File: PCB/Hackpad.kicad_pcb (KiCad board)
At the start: 2 copper layers, 86 x 50 mm, 11 parts, among them SW1 SW_Push, SW2 SW_Push, SW3 SW_Push, SW4 SW_Push, SW5 RotaryEncoder, U1 XIAO-RP2040-DIP, U2 SSD1306

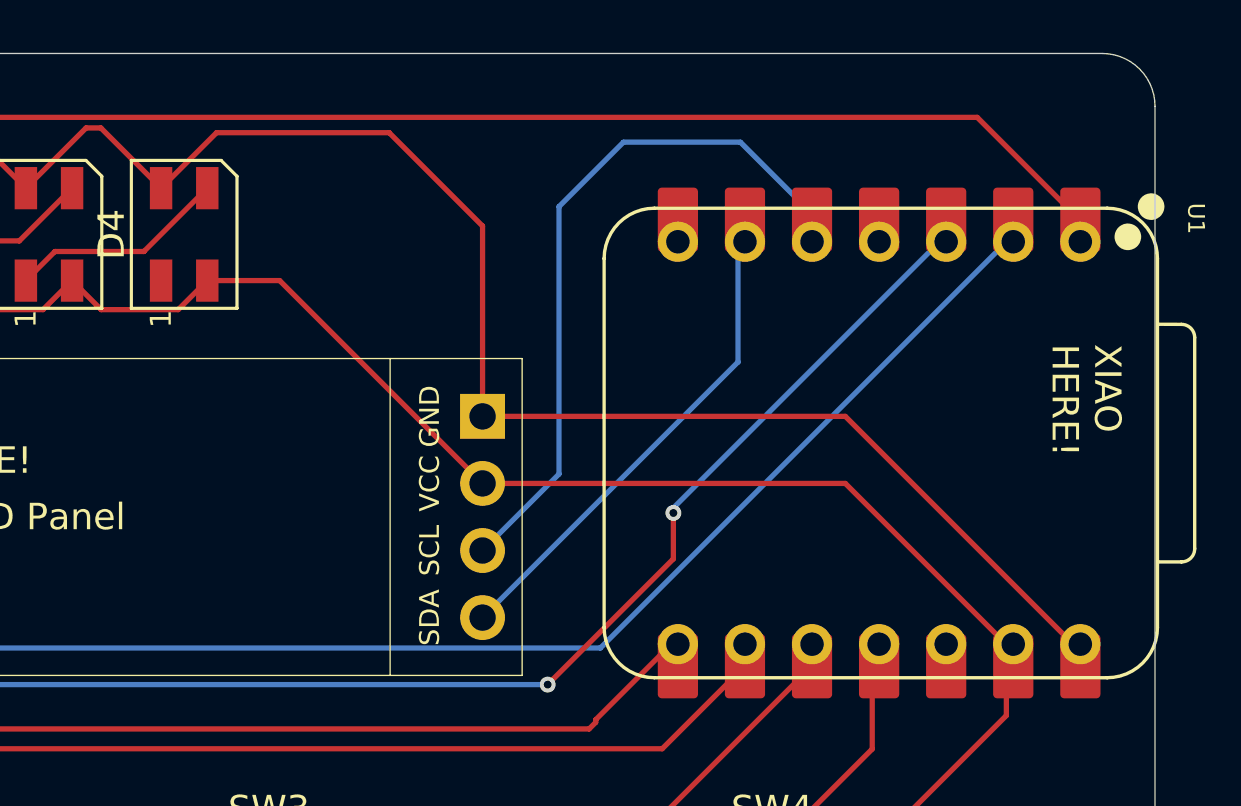
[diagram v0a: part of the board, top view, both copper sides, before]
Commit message: Connected the OLED to 3.3V instead of 5V
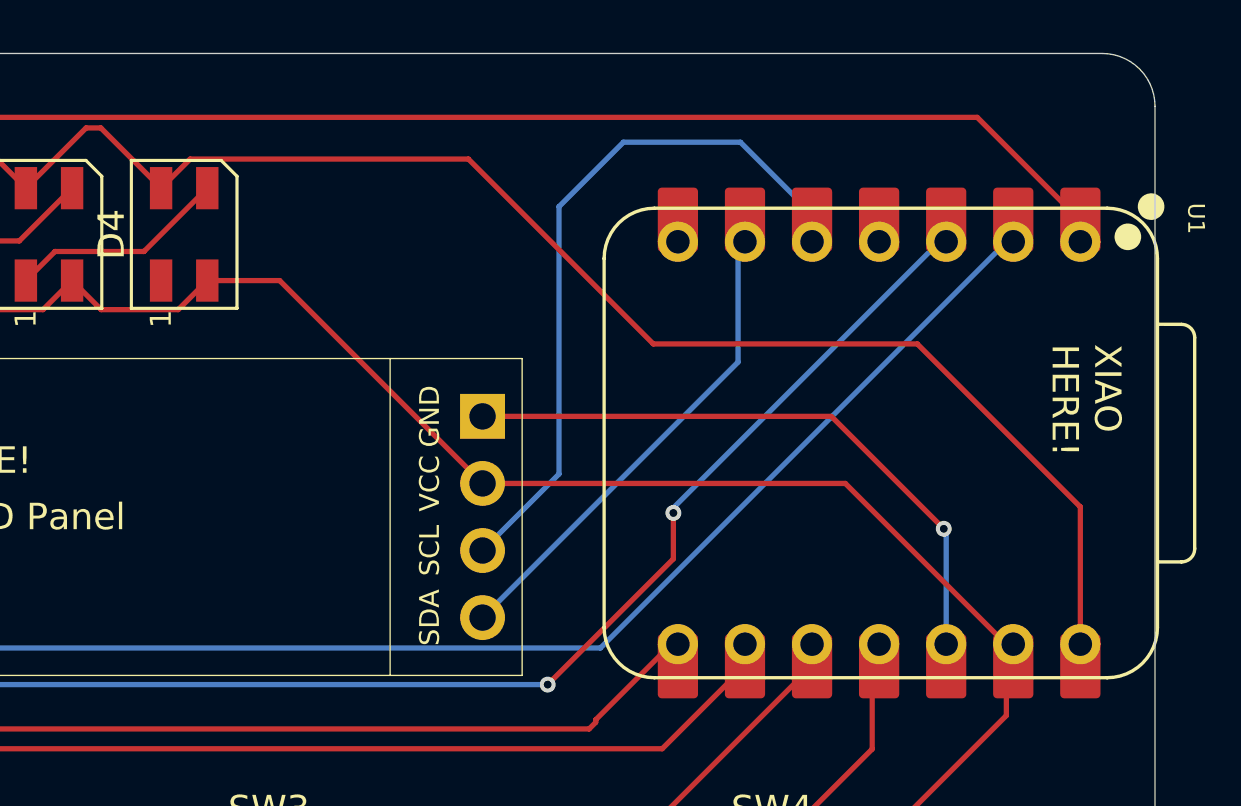
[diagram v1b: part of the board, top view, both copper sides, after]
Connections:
- U1 pad 12: unconnected-(U1-3V3-Pad12) -> +3.3V
- U2 pad 1: +5V -> +3.3V
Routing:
- net +3.3V: track 0.00 -> 23.6 mm, vias 0 -> 1
- net +5V: track 66.8 -> 65.0 mm
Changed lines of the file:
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@@
 	(net 12 "Net-(U1-GPIO28{slash}ADC2{slash}A2)")
 	(net 13 "Net-(U1-GPIO27{slash}ADC1{slash}A1)")
-	(net 14 "unconnected-(U1-3V3-Pad12)")
-	(net 15 "Net-(U1-GPIO7{slash}SCL)")
-	(net 16 "unconnected-(U1-GPIO29{slash}ADC3{slash}A3-Pad4)")
-	(net 17 "unconnected-(U1-GPIO0{slash}TX-Pad7)")
-	(net 18 "Net-(U1-GPIO6{slash}SDA)")
+	(net 14 "Net-(U1-GPIO7{slash}SCL)")
+	(net 15 "unconnected-(U1-GPIO29{slash}ADC3{slash}A3-Pad4)")
+	(net 16 "unconnected-(U1-GPIO0{slash}TX-Pad7)")
+	(net 17 "Net-(U1-GPIO6{slash}SDA)")
+	(net 18 "+3.3V")
 	(footprint "Seeed Studio XIAO Series Library:XIAO-RP2040-DIP"
 		(layer "F.Cu")
@@
 			(layers "F.Cu" "F.Mask")
 			(roundrect_rratio 0.1)
-			(net 16 "unconnected-(U1-GPIO29{slash}ADC3{slash}A3-Pad4)")
+			(net 15 "unconnected-(U1-GPIO29{slash}ADC3{slash}A3-Pad4)")
 			(pinfunction "GPIO29/ADC3/A3")
 			(pintype "passive")
@@
 			(layers "*.Cu" "*.Mask")
 			(remove_unused_layers no)
-			(net 16 "unconnected-(U1-GPIO29{slash}ADC3{slash}A3-Pad4)")
+			(net 15 "unconnected-(U1-GPIO29{slash}ADC3{slash}A3-Pad4)")
 			(pinfunction "GPIO29/ADC3/A3")
 			(pintype "passive")
@@
 			(layers "F.Cu" "F.Mask")
 			(roundrect_rratio 0.1)
-			(net 18 "Net-(U1-GPIO6{slash}SDA)")
+			(net 17 "Net-(U1-GPIO6{slash}SDA)")
 			(pinfunction "GPIO6/SDA")
 			(pintype "passive")
@@
 			(layers "*.Cu" "*.Mask")
 			(remove_unused_layers no)
-			(net 18 "Net-(U1-GPIO6{slash}SDA)")
+			(net 17 "Net-(U1-GPIO6{slash}SDA)")
 			(pinfunction "GPIO6/SDA")
 			(pintype "passive")
@@
 			(layers "F.Cu" "F.Mask")
 			(roundrect_rratio 0.1)
-			(net 15 "Net-(U1-GPIO7{slash}SCL)")
+			(net 14 "Net-(U1-GPIO7{slash}SCL)")
 			(pinfunction "GPIO7/SCL")
 			(pintype "passive")
@@
 			(layers "*.Cu" "*.Mask")
 			(remove_unused_layers no)
-			(net 15 "Net-(U1-GPIO7{slash}SCL)")
+			(net 14 "Net-(U1-GPIO7{slash}SCL)")
 			(pinfunction "GPIO7/SCL")
 			(pintype "passive")
@@
 			(layers "F.Cu" "F.Mask")
 			(roundrect_rratio 0.1)
-			(net 17 "unconnected-(U1-GPIO0{slash}TX-Pad7)")
+			(net 16 "unconnected-(U1-GPIO0{slash}TX-Pad7)")
 			(pinfunction "GPIO0/TX")
 			(pintype "passive")
@@
 			(layers "*.Cu" "*.Mask")
 			(remove_unused_layers no)
-			(net 17 "unconnected-(U1-GPIO0{slash}TX-Pad7)")
+			(net 16 "unconnected-(U1-GPIO0{slash}TX-Pad7)")
 			(pinfunction "GPIO0/TX")
 			(pintype "passive")
@@
 			(layers "*.Cu" "*.Mask")
 			(remove_unused_layers no)
-			(net 14 "unconnected-(U1-3V3-Pad12)")
+			(net 18 "+3.3V")
 			(pinfunction "3V3")
 			(pintype "passive")
@@
 			(layers "F.Cu" "F.Mask")
 			(roundrect_rratio 0.1)
-			(net 14 "unconnected-(U1-3V3-Pad12)")
+			(net 18 "+3.3V")
 			(pinfunction "3V3")
 			(pintype "passive")
@@
 			(layers "*.Cu" "*.Mask")
 			(remove_unused_layers no)
-			(net 4 "+5V")
+			(net 18 "+3.3V")
 			(pinfunction "VCC")
 			(pintype "passive")
@@
 			(layers "*.Cu" "*.Mask")
 			(remove_unused_layers no)
-			(net 18 "Net-(U1-GPIO6{slash}SDA)")
+			(net 17 "Net-(U1-GPIO6{slash}SDA)")
 			(pinfunction "SDA")
 			(pintype "passive")
@@
 			(layers "*.Cu" "*.Mask")
 			(remove_unused_layers no)
-			(net 15 "Net-(U1-GPIO7{slash}SCL)")
+			(net 14 "Net-(U1-GPIO7{slash}SCL)")
 			(pinfunction "SCL")
 			(pintype "passive")
@@
 	)
 	(segment
-		(start 129.53375 60.53375)
-		(end 129.53375 67.7425)
-		(width 0.2)
-		(layer "F.Cu")
-		(net 4)
-	)
-	(segment
-		(start 117.36 59.1)
-		(end 119.46 57)
+		(start 102 59.1)
+		(end 103.101 57.999)
 		(width 0.2)
 		(layer "F.Cu")
@@
 	)
 	(segment
-		(start 102 59.1)
-		(end 103.101 57.999)
+		(start 115.08 56.82)
+		(end 117.36 59.1)
 		(width 0.2)
 		(layer "F.Cu")
@@
 	)
 	(segment
-		(start 115.08 56.82)
-		(end 117.36 59.1)
+		(start 136 65)
+		(end 146 65)
 		(width 0.2)
 		(layer "F.Cu")
@@
 	)
 	(segment
+		(start 117.36 59.1)
+		(end 118.461 57.999)
+		(width 0.2)
+		(layer "F.Cu")
+		(net 4)
+	)
+	(segment
 		(start 108.26 57.96)
 		(end 111.1 57.96)
@@
 	)
 	(segment
-		(start 111.1 57.96)
-		(end 112.24 59.1)
+		(start 146 65)
+		(end 152.1715 71.1715)
 		(width 0.2)
 		(layer "F.Cu")
@@
 	)
 	(segment
-		(start 119.46 57)
-		(end 126 57)
+		(start 152.1715 71.1715)
+		(end 152.1715 76.37)
 		(width 0.2)
 		(layer "F.Cu")
@@
 	)
 	(segment
-		(start 151.91 76.38)
-		(end 143.2725 67.7425)
+		(start 111.1 57.96)
+		(end 112.24 59.1)
 		(width 0.2)
 		(layer "F.Cu")
@@
 	)
 	(segment
-		(start 107.12 59.1)
-		(end 108.26 57.96)
+		(start 128.999 57.999)
+		(end 136 65)
 		(width 0.2)
 		(layer "F.Cu")
@@
 	)
 	(segment
-		(start 143.2725 67.7425)
-		(end 129.53375 67.7425)
+		(start 107.12 59.1)
+		(end 108.26 57.96)
 		(width 0.2)
 		(layer "F.Cu")
@@
 	)
 	(segment
-		(start 112.24 59.1)
-		(end 114.52 56.82)
+		(start 118.461 57.999)
+		(end 128.999 57.999)
 		(width 0.2)
 		(layer "F.Cu")
@@
 	)
 	(segment
-		(start 126 57)
-		(end 129.53375 60.53375)
+		(start 112.24 59.1)
+		(end 114.52 56.82)
 		(width 0.2)
 		(layer "F.Cu")
@@
 		(width 0.2)
 		(layer "B.Cu")
-		(net 15)
+		(net 14)
 	)
 	(segment
@@
 		(width 0.2)
 		(layer "B.Cu")
-		(net 15)
+		(net 14)
 	)
 	(segment
@@
 		(width 0.2)
 		(layer "B.Cu")
-		(net 18)
+		(net 17)
 	)
 	(segment
@@
 		(width 0.2)
 		(layer "B.Cu")
-		(net 18)
+		(net 17)
 	)
 	(segment
@@
 		(width 0.2)
 		(layer "B.Cu")
-		(net 18)
+		(net 17)
 	)
 	(segment
@@
 		(width 0.2)
 		(layer "B.Cu")
-		(net 18)
+		(net 17)
 	)
 	(segment
@@
 		(width 0.2)
 		(layer "B.Cu")
-		(net 18)
+		(net 17)
 	)
 	(segment
@@
 		(width 0.2)
 		(layer "B.Cu")
+		(net 17)
+	)
+	(segment
+		(start 142.7425 67.7425)
+		(end 147 72)
+		(width 0.2)
+		(layer "F.Cu")
+		(net 18)
+	)
+	(segment
+		(start 129.53375 67.7425)
+		(end 142.7425 67.7425)
+		(width 0.2)
+		(layer "F.Cu")
+		(net 18)
+	)
+	(via
+		(at 147 72)
+		(size 0.6)
+		(drill 0.3)
+		(layers "F.Cu" "B.Cu")
+		(net 18)
+	)
+	(segment
+		(start 147 72)
+		(end 147.0915 72.0915)
+		(width 0.2)
+		(layer "B.Cu")
+		(net 18)
+	)
+	(segment
+		(start 147.0915 72.0915)
+		(end 147.0915 76.37)
+		(width 0.2)
+		(layer "B.Cu")

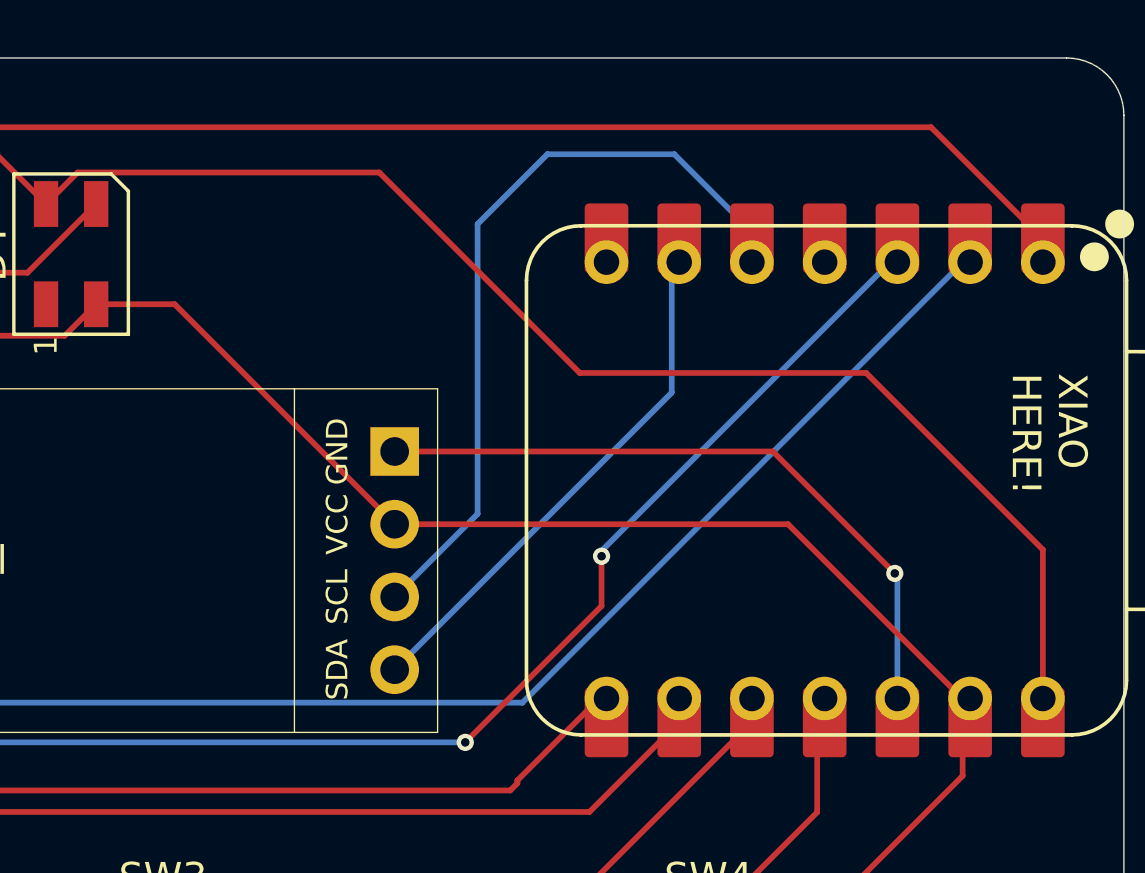
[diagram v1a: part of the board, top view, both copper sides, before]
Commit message: Rearranged pins on the OLED
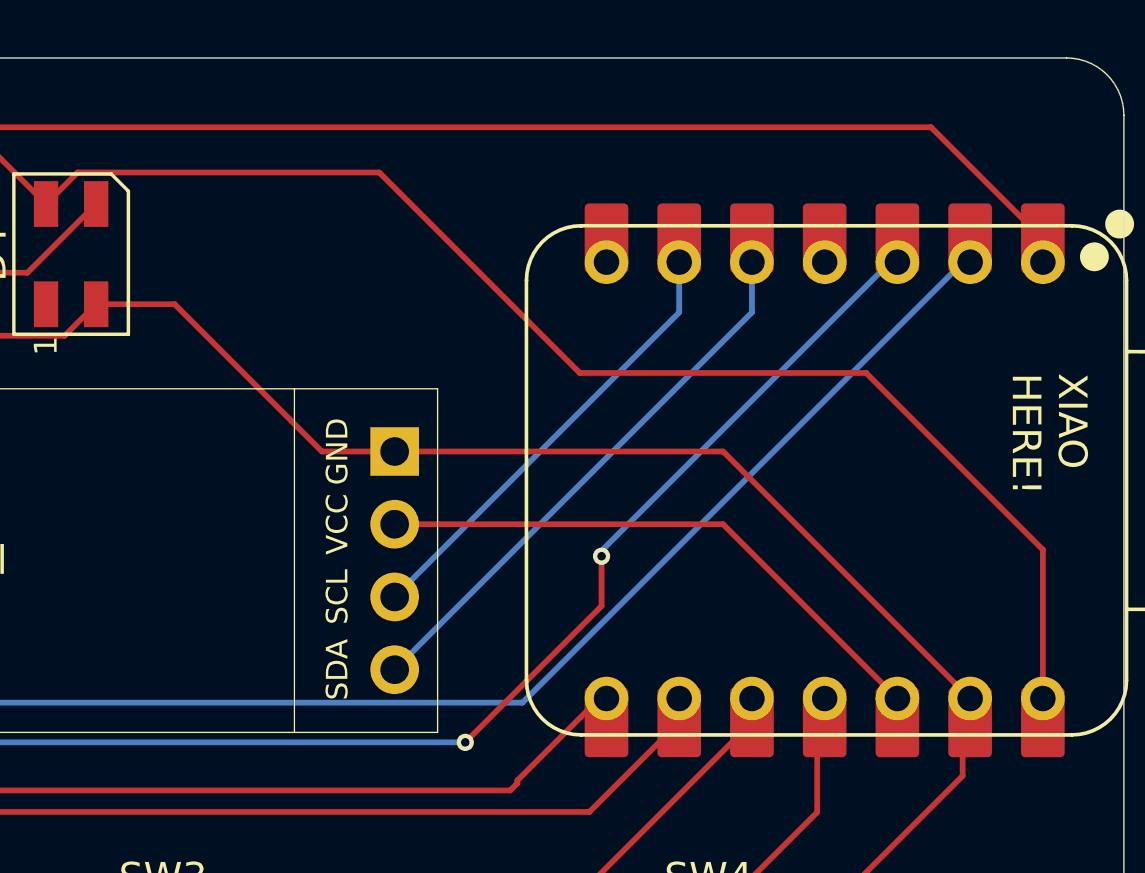
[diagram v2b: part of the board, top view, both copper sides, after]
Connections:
- U2 pad 1: +3.3V -> GND
- U2 pad 2: GND -> +3.3V
- U2 pad 3: Net-(U1-GPIO6/SDA) -> Net-(U1-GPIO7/SCL)
- U2 pad 4: Net-(U1-GPIO7/SCL) -> Net-(U1-GPIO6/SDA)
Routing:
- net Net-(U1-GPIO6/SDA): track 26.9 -> 20.7 mm
- net +3.3V: track 23.6 -> 20.1 mm, vias 1 -> 0
- net Net-(U1-GPIO7/SCL): track 18.2 -> 15.8 mm
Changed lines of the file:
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@@
 			(layers "*.Cu" "*.Mask")
 			(remove_unused_layers no)
-			(net 18 "+3.3V")
+			(net 3 "GND")
 			(pinfunction "VCC")
 			(pintype "passive")
@@
 			(layers "*.Cu" "*.Mask")
 			(remove_unused_layers no)
-			(net 3 "GND")
+			(net 18 "+3.3V")
 			(pinfunction "GND")
 			(pintype "passive")
@@
 			(layers "*.Cu" "*.Mask")
 			(remove_unused_layers no)
-			(net 17 "Net-(U1-GPIO6{slash}SDA)")
+			(net 14 "Net-(U1-GPIO7{slash}SCL)")
 			(pinfunction "SDA")
 			(pintype "passive")
@@
 			(layers "*.Cu" "*.Mask")
 			(remove_unused_layers no)
-			(net 14 "Net-(U1-GPIO7{slash}SCL)")
+			(net 17 "Net-(U1-GPIO6{slash}SDA)")
 			(pinfunction "SCL")
 			(pintype "passive")
@@
 	)
 	(segment
-		(start 143.2725 70.2825)
-		(end 149.37 76.38)
+		(start 121.85125 62.6)
+		(end 126.99375 67.7425)
 		(width 0.2)
 		(layer "F.Cu")
@@
 	)
 	(segment
+		(start 141.004 67.7425)
+		(end 149.6315 76.37)
+		(width 0.2)
+		(layer "F.Cu")
+		(net 3)
+	)
+	(segment
+		(start 129.53375 67.7425)
+		(end 141.004 67.7425)
+		(width 0.2)
+		(layer "F.Cu")
+		(net 3)
+	)
+	(segment
 		(start 103.75 62.6)
 		(end 104.851 63.701)
@@
 	)
 	(segment
-		(start 129.53375 70.2825)
-		(end 143.2725 70.2825)
-		(width 0.2)
-		(layer "F.Cu")
-		(net 3)
-	)
-	(segment
 		(start 113.99 62.6)
 		(end 115.091 63.701)
@@
 	)
 	(segment
+		(start 126.99375 67.7425)
+		(end 129.53375 67.7425)
+		(width 0.2)
+		(layer "F.Cu")
+		(net 3)
+	)
+	(segment
 		(start 108.87 62.6)
 		(end 109.971 63.701)
-		(width 0.2)
-		(layer "F.Cu")
-		(net 3)
-	)
-	(segment
-		(start 121.85125 62.6)
-		(end 129.53375 70.2825)
 		(width 0.2)
 		(layer "F.Cu")
@@
 	)
 	(segment
-		(start 129.53375 75.3625)
-		(end 139.21 65.68625)
+		(start 139.4715 62.88475)
+		(end 129.53375 72.8225)
 		(width 0.2)
 		(layer "B.Cu")
@@
 	)
 	(segment
-		(start 139.21 65.68625)
-		(end 139.21 61.14)
+		(start 139.4715 61.13)
+		(end 139.4715 62.88475)
 		(width 0.2)
 		(layer "B.Cu")
@@
 	)
 	(segment
-		(start 132.43 69.92625)
-		(end 132.43 59.8)
+		(start 142.0115 62.88475)
+		(end 142.0115 61.13)
 		(width 0.2)
 		(layer "B.Cu")
@@
 	)
 	(segment
-		(start 129.53375 72.8225)
-		(end 132.43 69.92625)
+		(start 129.53375 75.3625)
+		(end 142.0115 62.88475)
 		(width 0.2)
 		(layer "B.Cu")
@@
 	)
 	(segment
-		(start 134.87 57.36)
-		(end 139.3 57.36)
-		(width 0.2)
-		(layer "B.Cu")
-		(net 17)
-	)
-	(segment
-		(start 139.3 57.36)
-		(end 141.75 59.81)
-		(width 0.2)
-		(layer "B.Cu")
-		(net 17)
-	)
-	(segment
-		(start 132.43 59.8)
-		(end 134.87 57.36)
-		(width 0.2)
-		(layer "B.Cu")
-		(net 17)
-	)
-	(segment
-		(start 142.7425 67.7425)
-		(end 147 72)
+		(start 129.53375 70.2825)
+		(end 141.004 70.2825)
 		(width 0.2)
 		(layer "F.Cu")
@@
 	)
 	(segment
-		(start 129.53375 67.7425)
-		(end 142.7425 67.7425)
+		(start 141.004 70.2825)
+		(end 147.0915 76.37)
 		(width 0.2)
 		(layer "F.Cu")
 		(net 18)
 	)
-	(via
-		(at 147 72)
-		(size 0.6)
-		(drill 0.3)
-		(layers "F.Cu" "B.Cu")
-		(net 18)
-	)
-	(segment
-		(start 147 72)
-		(end 147.0915 72.0915)
-		(width 0.2)
-		(layer "B.Cu")
-		(net 18)
-	)
-	(segment
-		(start 147.0915 72.0915)
-		(end 147.0915 76.37)
-		(width 0.2)
-		(layer "B.Cu")
-		(net 18)
-	)
